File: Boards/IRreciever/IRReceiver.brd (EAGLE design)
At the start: 78.5 x 49 mm, 14 parts, among them IC1 MEGA8-P, Q1 BSS138

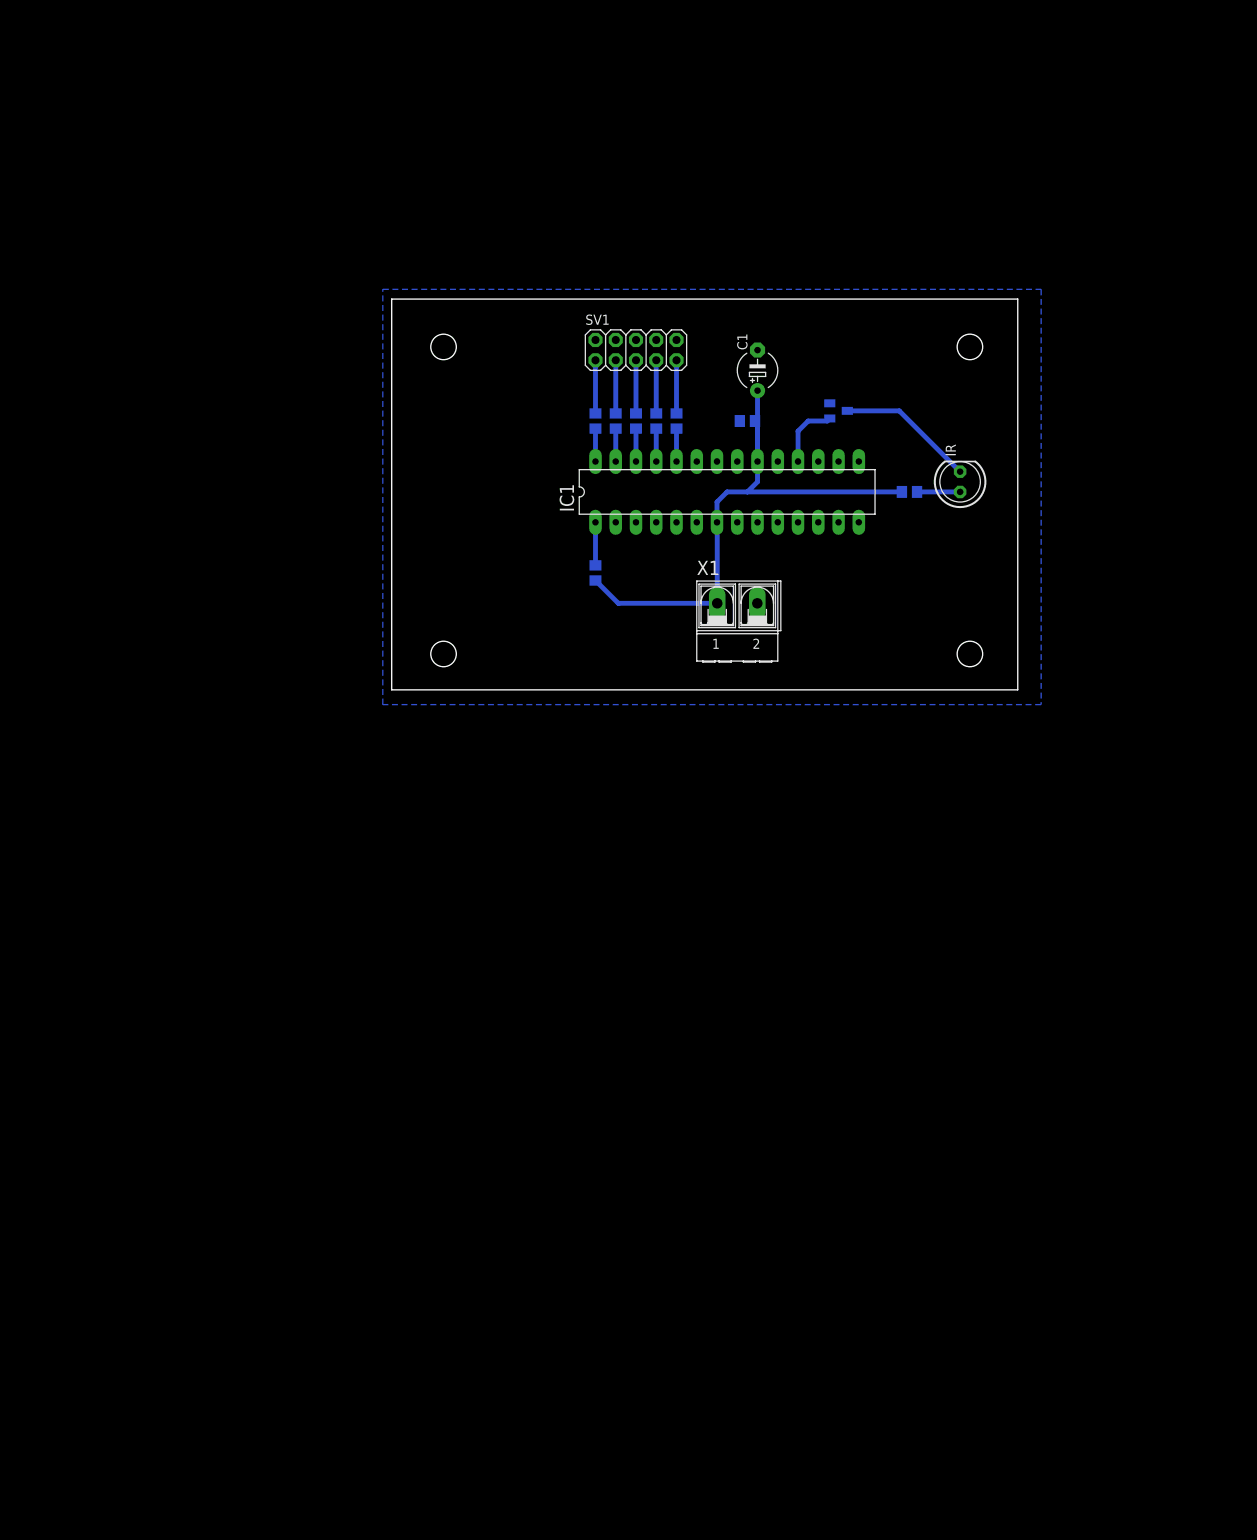
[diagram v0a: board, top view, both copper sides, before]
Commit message: schematic of IR receiver
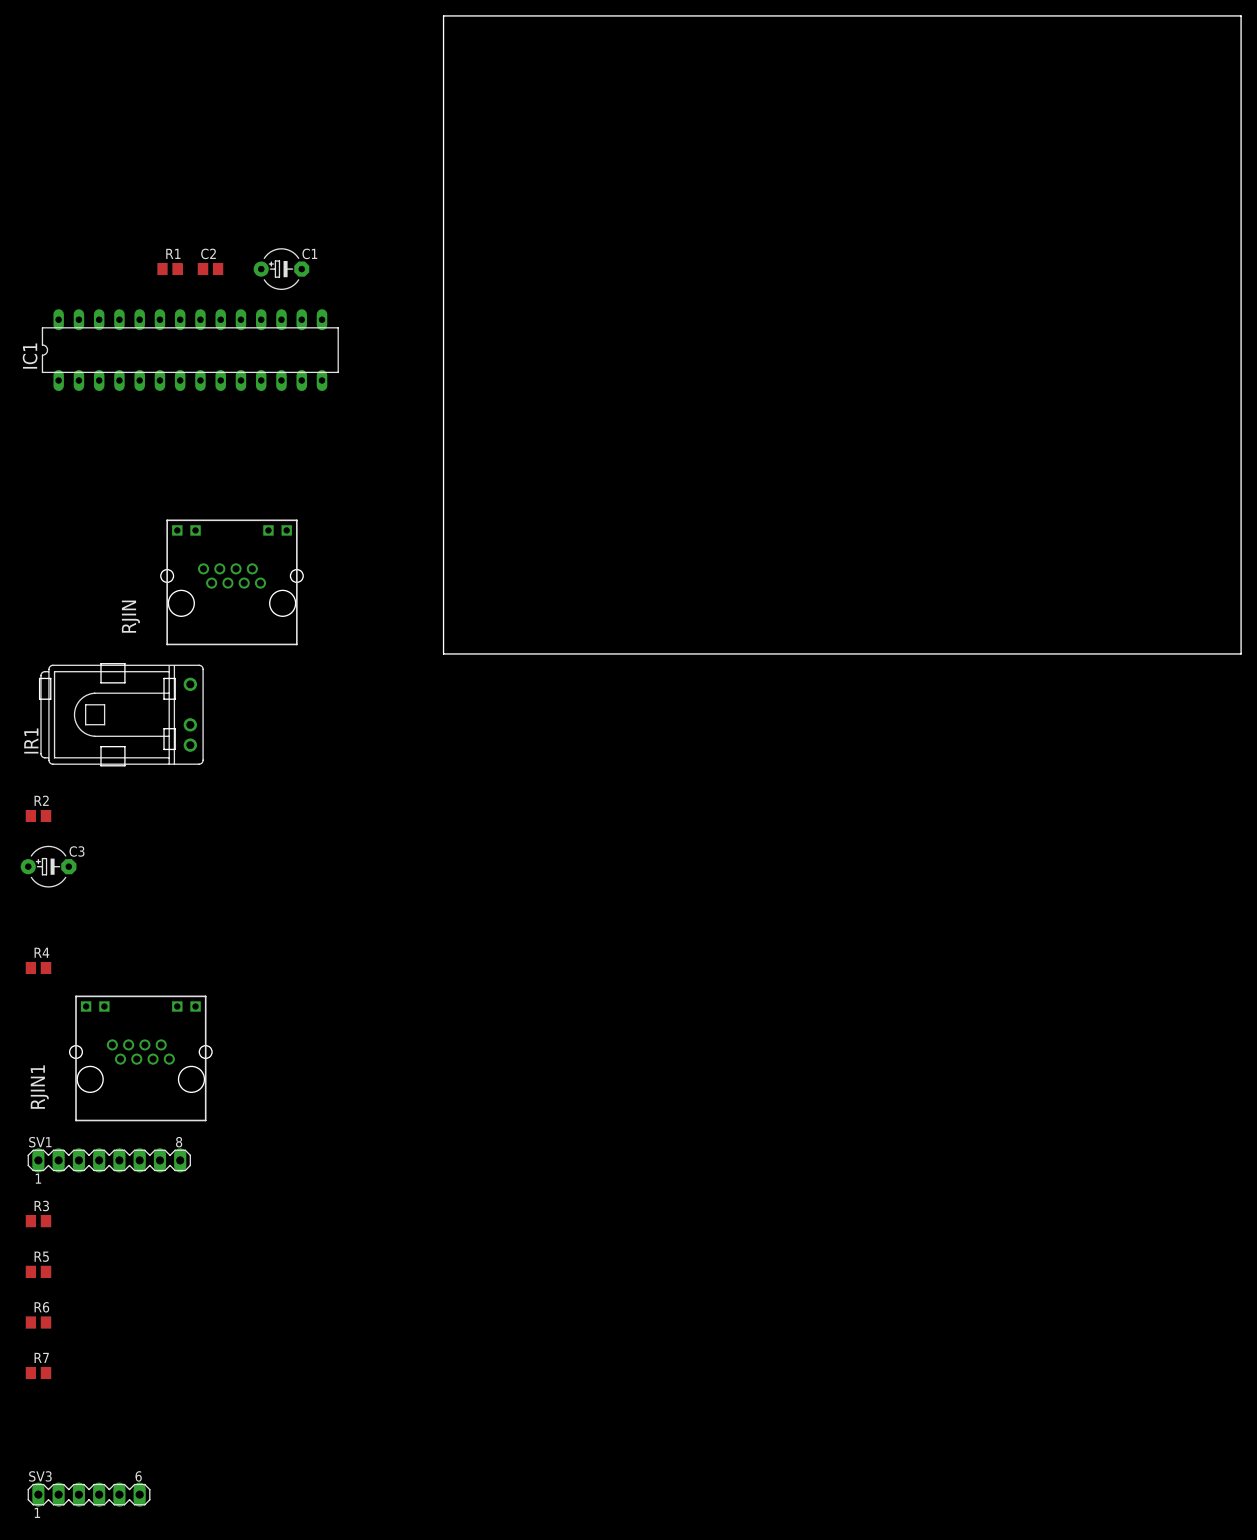
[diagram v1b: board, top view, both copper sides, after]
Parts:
- removed IR: (no value), led:LED5MM
- removed Q1: BSS138, transistor-small-signal:SOT23
- removed X1: (no value), con-ptr500:AK500/2-H
- added C3: 22uF, rcl:E5-5
- added IR1: TSOP1736TB1, telefunken:TSOP17_TB1
- added RJIN, RJIN1: 8P8CLED, rj45:8P8CLED
- added SV3: (no value), con-lstb:MA06-1
- R2: value 150 -> 100
- R4: value 1k -> 10k
- SV1: device pinhead:2X05 -> con-lstb:MA08-1
- moved R7 138.3 mm to (-50.8, -90.2), flipped to the top, turned to 0 degrees
- moved R6 134.2 mm to (-50.8, -83.8), flipped to the top, turned to 0 degrees
- moved R5 130.4 mm to (-50.8, -77.5), flipped to the top, turned to 0 degrees
- moved R3 128.3 mm to (-50.8, -71.1), flipped to the top, turned to 0 degrees
- moved SV1 121.2 mm to (-41.9, -63.5)
- moved R2 116.5 mm to (-50.8, -20.3), flipped to the top
- moved R4 103.5 mm to (-50.8, -39.4), flipped to the top, turned to 0 degrees
- moved C2 70.0 mm to (-29.2, 48.3), flipped to the top
- moved IC1 69.6 mm to (-31.8, 38.1)
- moved R1 65.5 mm to (-34.3, 48.3), flipped to the top, turned to 0 degrees
- moved C1 61.0 mm to (-20.3, 48.3), turned to 0 degrees
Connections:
- removed net N$7: IC1.26, R5.1
- removed net N$8: IC1.27, R6.1
- removed net N$9: IC1.28, R7.1
- new net 1: IC1.23, RJIN.1, RJIN1.1, SV1.1
- new net 2: IC1.24, RJIN.2, RJIN1.2, SV1.2
- new net 3: IC1.25, RJIN.3, RJIN1.3, SV1.3
- new net 4: IC1.26, RJIN.4, RJIN1.4, SV1.4
- new net 5: IC1.27, RJIN.5, RJIN1.5, SV1.5
- new net LED1IN: R7.2, RJIN.LED1VCC
- new net LED1OUT: R5.2, RJIN1.LED1VCC
- new net LED2IN: R6.2, RJIN.LED2VCC
- new net LED2OUT: R3.2, RJIN1.LED2VCC
- new net LEDSTATUS: IC1.2, SV3.6
- new net TSOP: IC1.4, IR1.VO, R4.1
- net GND: now also C3.-, IR1.GND, RJIN.7, RJIN.LED1GND, RJIN.LED2GND, RJIN1.7, RJIN1.LED1GND, RJIN1.LED2GND, SV1.7; no longer Q1.2, SV1.10, SV1.2, SV1.4, SV1.6, SV1.8, X1.2
- net LED1: now also IC1.5, SV3.1; no longer R3.2, SV1.9
- net LED2: now also IC1.6, SV3.2; no longer R4.2, SV1.7
- net LED3: now also IC1.11, SV3.3; no longer R5.2, SV1.5
- net LED4: now also IC1.12, SV3.4; no longer R6.2, SV1.3
- net LED5: now also IC1.13, SV3.5; no longer R7.2, SV1.1
- net N$1: now also C3.+, IR1.VS; no longer IR.A
- net N$3: now also IC1.19, R3.1; no longer IR.K, Q1.3
- net N$4: now also R5.1; no longer Q1.1
- net N$5: now also IC1.17, R6.1; no longer IC1.24, R3.1
- net N$6: now also IC1.16, R7.1; no longer IC1.25, R4.1
- net VCC: now also R4.2, RJIN.8, RJIN1.8, SV1.8; no longer X1.1
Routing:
- net VCC: track 71.8 -> 0.00 mm
- net N$3: track 17.3 -> 0.00 mm
- net N$4: track 8.45 -> 0.00 mm
- net LED5: track 6.67 -> 0.00 mm
- net LED4: track 6.67 -> 0.00 mm
- net LED3: track 6.67 -> 0.00 mm
- net LED2: track 6.67 -> 0.00 mm
- net LED1: track 6.67 -> 0.00 mm
- net N$2: track 5.40 -> 0.00 mm
- net N$1: track 5.40 -> 0.00 mm
- net N$9: track 4.13 -> 0.00 mm
- net N$8: track 4.13 -> 0.00 mm
- net N$7: track 4.13 -> 0.00 mm
- net N$6: track 4.13 -> 0.00 mm
- net N$5: track 4.13 -> 0.00 mm
- removed copper zone on layer 16, net GND
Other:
- board size 78.5 x 49 mm -> 100 x 80 mm
